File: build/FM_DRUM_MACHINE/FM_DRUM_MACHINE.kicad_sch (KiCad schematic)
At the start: 292 parts, among them J1 PJ-102A, J2 KICK_BUFFEREDOUT, J3 SNARE_BUFFEREDOUT, J4 HATS_BUFFEREDOUT, J5 TOMS_BUFFEREDOUT, J6 LINE_OUT, Q1 BC547, Q2 BC557, SW1 STEP1, SW10 STEP10, SW11 STEP11, SW12 STEP12, SW13 STEP13, SW14 STEP14, SW15 STEP15, SW16 STEP16, SW17 KICK_TRIG, SW18 SNARE_TRIG, SW19 CHAT_TRIG, SW2 STEP2, SW20 OHAT_TRIG, SW21 LOTOM_TRIG, SW22 HITOM_TRIG, SW23 PLAY/PAUSE, SW24 RECORD, SW25 SELECT, SW26 SW_DPDT_x2, SW27 SW_DPDT_x2, SW3 STEP3, SW4 STEP4, SW5 STEP5, SW6 STEP6, SW7 STEP7, SW8 STEP8, SW9 STEP9, U1 6N138, U10 TL072, U11 TL074, U12 TL072, U13 TL074, U14 TL074, U15 TL072, U16 TL072, U2 TL072, U3 TL072, U4 TL074, U5 MAX7221xNG, U6 CD74HC4067M, U7 CD74HC4067M, U8 AMS1117-5.0, U9 AMS1117-3.3

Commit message: v0.5.3
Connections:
- net HATS_DCBIAS_OUT is gone; now on net HATSBUFFER_IN: C5.1, R3.1, R4.2, R40.1
- net KICK_DCBIAS_OUT is gone; now on net KICKBUFFER_IN: C3.1, R38.1, R49.1, R50.2
- net SNARE_DCBIAS_OUT is gone; now on net SNAREBUFFER_IN: C4.1, R1.1, R2.2, R39.1
- net TOMS_DCBIAS_OUT is gone; now on net TOMSBUFFER_IN: C6.1, R41.1, R5.1, R6.2
- net HATSBUFFER_IN: no longer C5.2, RV33.3
- net KICKBUFFER_IN: no longer C3.2, RV46.3
- net SNAREBUFFER_IN: no longer RV40.3
- net TOMSBUFFER_IN: no longer C6.2, RV35.3
- new net HATS_DCBIAS_IN: C5.2, RV33.3
- new net KICK_DCBIAS_IN: C3.2, RV46.3
- new net SNARE_DCBIAS_IN: RV40.3
- new net TOMS_DCBIAS_IN: C6.2, RV35.3

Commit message: v0.5.5
- Drive section modified based on testing
- LPF/HPF Based on testing
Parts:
- removed D55, D56: 1N4148, Diode_THT:D_DO-35_SOD27_P5.08mm_Vertical_KathodeUp, symbol Diode:1N4148
- removed R42, R43, R47, R48, R49: 10k, PCM_4ms_Resistor:R_Axial_DIN0207_L6.3mm_D2.5mm_P7.62mm_Horizontal, symbol Device:R
- added R13: 820R, PCM_4ms_Resistor:R_Axial_DIN0207_L6.3mm_D2.5mm_P7.62mm_Horizontal, symbol Device:R
- added R14, R15: 330R, PCM_4ms_Resistor:R_Axial_DIN0207_L6.3mm_D2.5mm_P7.62mm_Horizontal, symbol Device:R
- D3: value 1N4148 -> RED LED
- D4: value 1N4148 -> 1N4007
- R1, R3, R5: value 10k -> 820R
- R2, R4, R50, R6: value 10k -> 330R
- R52: value 2k -> 680R
- R53, R56, R60, R73: value 200k -> 220k
- R58, R64: value 6k8 -> 10k
- RV29: value R_Potentiometer -> 100k
- RV38: value 20k -> B20k
- RV39: value 1k -> A1k
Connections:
- net 12V: no longer R1.2, R3.2, R5.2
- net GND: no longer R2.1, R4.1, R50.1, R6.1
- net HATSBUFFER_IN: no longer R3.1
- net SNAREBUFFER_IN: no longer R1.1
- net SOFTCLIP_OUT: now also D3.2 (A), D4.1 (K); no longer D4.2 (A)
- net TOMSBUFFER_IN: no longer R5.1
- net VGND: now also R2.1, R4.1, R5.2, R50.1, R6.1, RV38.3, U2.3 (+), U2.5 (+), R14.1, R15.1; no longer R52.1, RV27.1, RV29.1, TRIM1.1 (Left)
- net at D3.1 (K), R51.2, U3.2 (-): now also D4.2 (A), R52.2; no longer RV38.3
- net at RV27.4, U11.6 (-), U11.7: now also R13.1, R13.2
- net at U4.1, U4.2 (-): now also R1.1; no longer RV28.1
- net at RV28.4, U4.6 (-), U4.7: now also R3.1, R3.2
- net at RV38.1, RV38.2: now also R52.1; no longer R52.2
- new net: R5.1, RV27.1
- new net: R15.2, TRIM1.1 (Left)
- new net: R14.2, RV29.1
- new net: R1.2, RV28.1
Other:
- moved on the sheet: C3, C4, C5, C6, C82, C83, D3, D57, D58, D59, D60, D61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

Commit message: v0.6
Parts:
- R88: value 20k -> 33k
- RV31: value 20k -> 10k
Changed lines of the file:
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@@
 			)
 		)
-		(property "Value" "20k"
+		(property "Value" "33k"
 			(at 659.13 223.266 90)
 			(effects
@@
 			)
 		)
-		(property "Value" "20k"
+		(property "Value" "10k"
 			(at 661.67 234.9499 0)
 			(effects

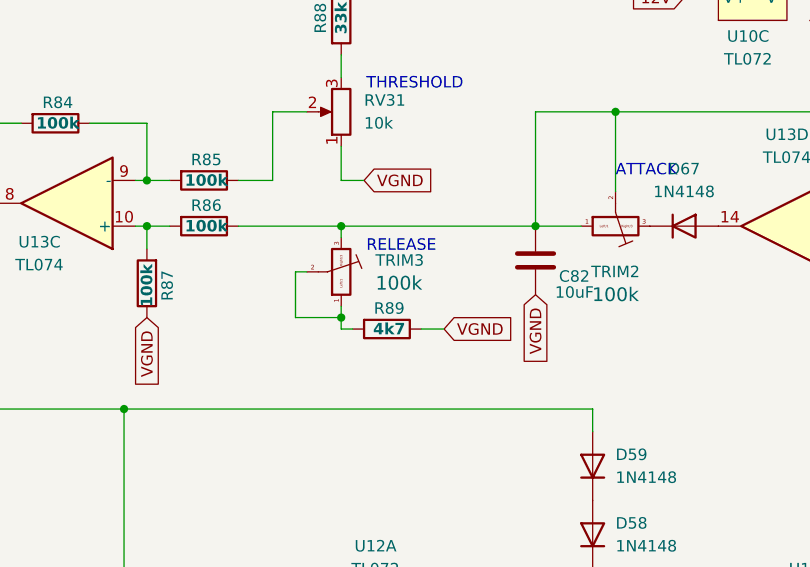
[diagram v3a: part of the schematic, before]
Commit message: Sound Design Edits
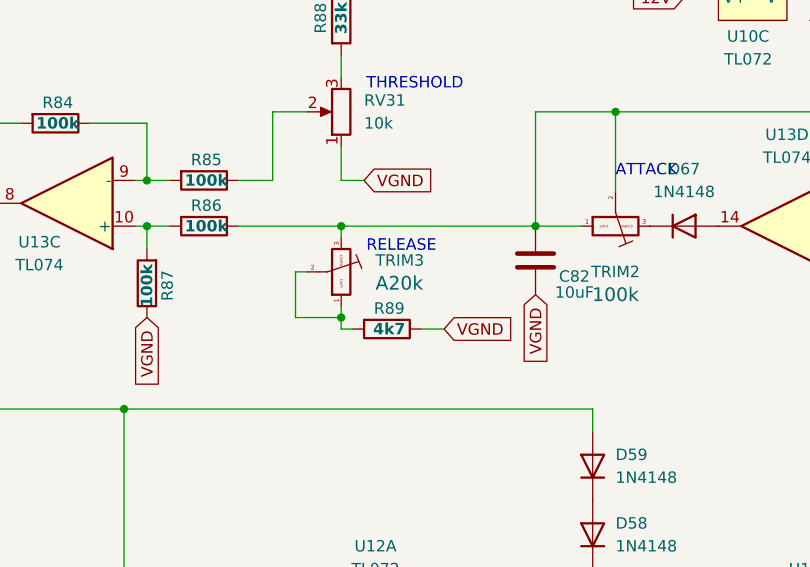
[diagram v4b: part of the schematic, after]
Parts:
- TRIM3: Display 100k -> A20k
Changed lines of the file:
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@@
 			)
 		)
-		(property "Display" "100k"
+		(property "Display" "A20k"
 			(at 662.94 252.7299 0)
 			(effects

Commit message: Schematic Changes
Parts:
- removed C65, C66, C67, C68: 10nF, PCM_4ms_Capacitor:C_Disc_P5.08mm, symbol Device:C
- removed RV23: OHAT_DECAY, DIYSynthMNL:Potentiometer_RV09_BigPads, symbol Device:R_Potentiometer
- removed RV24: OHAT_TIMBRE, DIYSynthMNL:Potentiometer_RV09_BigPads, symbol Device:R_Potentiometer
- removed RV25: OHAT_PITCH, DIYSynthMNL:Potentiometer_RV09_BigPads, symbol Device:R_Potentiometer
- removed RV26: OHAT_FMFREQ, DIYSynthMNL:Potentiometer_RV09_BigPads, symbol Device:R_Potentiometer
- RV11: value CHAT_DECAY -> HAT_DECAY
- RV12: value CHAT_TIMBRE -> HAT_TIMBRE
- RV13: value CHAT_PITCH -> HAT_TONE
- RV14: value CHAT_FMFREQ -> HAT_RESONANCE
- RV17: value LOTOM_PITCH -> LOTOM_TUNE
- RV18: value LOTOM_FMFREQ -> LOTOM_PITCHENVTIME
- RV21: value HITOM_PITCH -> HITOM_TUNE
- RV22: value HITOM_FMFREQ -> HITOM_PITCHENVTIME
- RV3: value KICK_PITCH -> KICK_TUNE
- RV5: value KICK_FMFREQ -> KICK_PITCHENVTIME
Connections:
- net OHAT_FMFREQ is gone; now on net LOTOM_DECAY: U7.9 (I0)
- net HITOM_DECAY: now also U7.5 (I4); no longer U7.4 (I5)
- net HITOM_PITCH: now also U7.4 (I5); no longer U7.3 (I6)
- net HITOM_PUNCH: now also U7.3 (I6); no longer U7.2 (I7)
- net LOTOM_DECAY: no longer U7.8 (I1)
- net LOTOM_PUNCH: now also U7.7 (I2); no longer U7.6 (I3)
- net CHAT_DECAY renamed HAT_DECAY
- net CHAT_FMFREQ renamed HAT_RESONANCE
- net CHAT_PITCH renamed HAT_TONE
- net CHAT_TIMBRE renamed HAT_TIMBRE
- net HITOM_FMFREQ renamed HITOM_PITCHENVTIME
- net HITOM_PITCHENVTIME: now also U7.2 (I7); no longer U7.23 (I8)
- net KICK_FMFREQ renamed KICK_PITCHENVTIME
- net KICK_PITCH renamed KICK_TUNE
- net LOTOM_FMFREQ renamed LOTOM_PITCHENVTIME
- net LOTOM_PITCHENVTIME: now also U7.6 (I3); no longer U7.5 (I4)
- net LOTOM_PITCH renamed LOTOM_TUNE
- net LOTOM_TUNE: now also U7.8 (I1); no longer U7.7 (I2)
- net OHAT_DECAY: no longer names the net of U6.18 (I13)
- net OHAT_PITCH: no longer names the net of U6.17 (I14)
- net OHAT_TIMBRE: no longer names the net of U6.16 (I15)
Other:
- note added: "HAT"
- note removed: "CHAT"
- note removed: "OHAT"

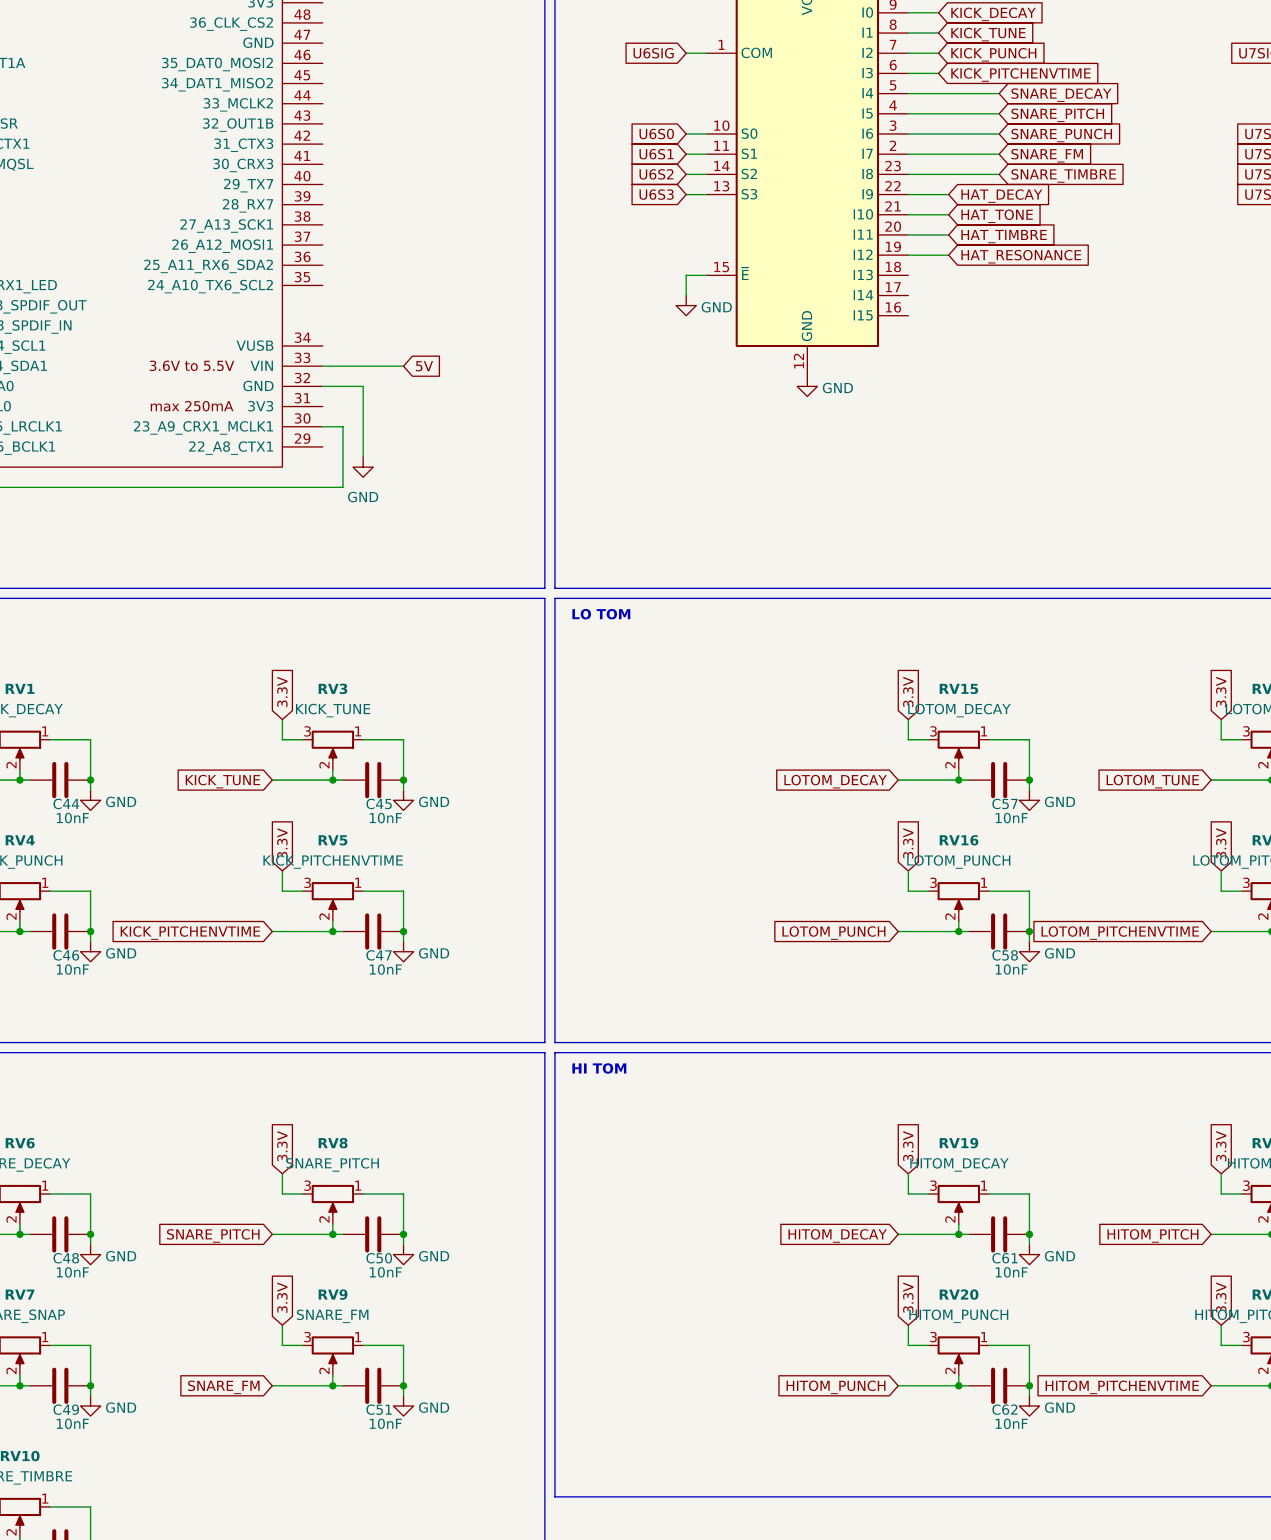
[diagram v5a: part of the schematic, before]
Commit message: Hi Hats added to ENGINE
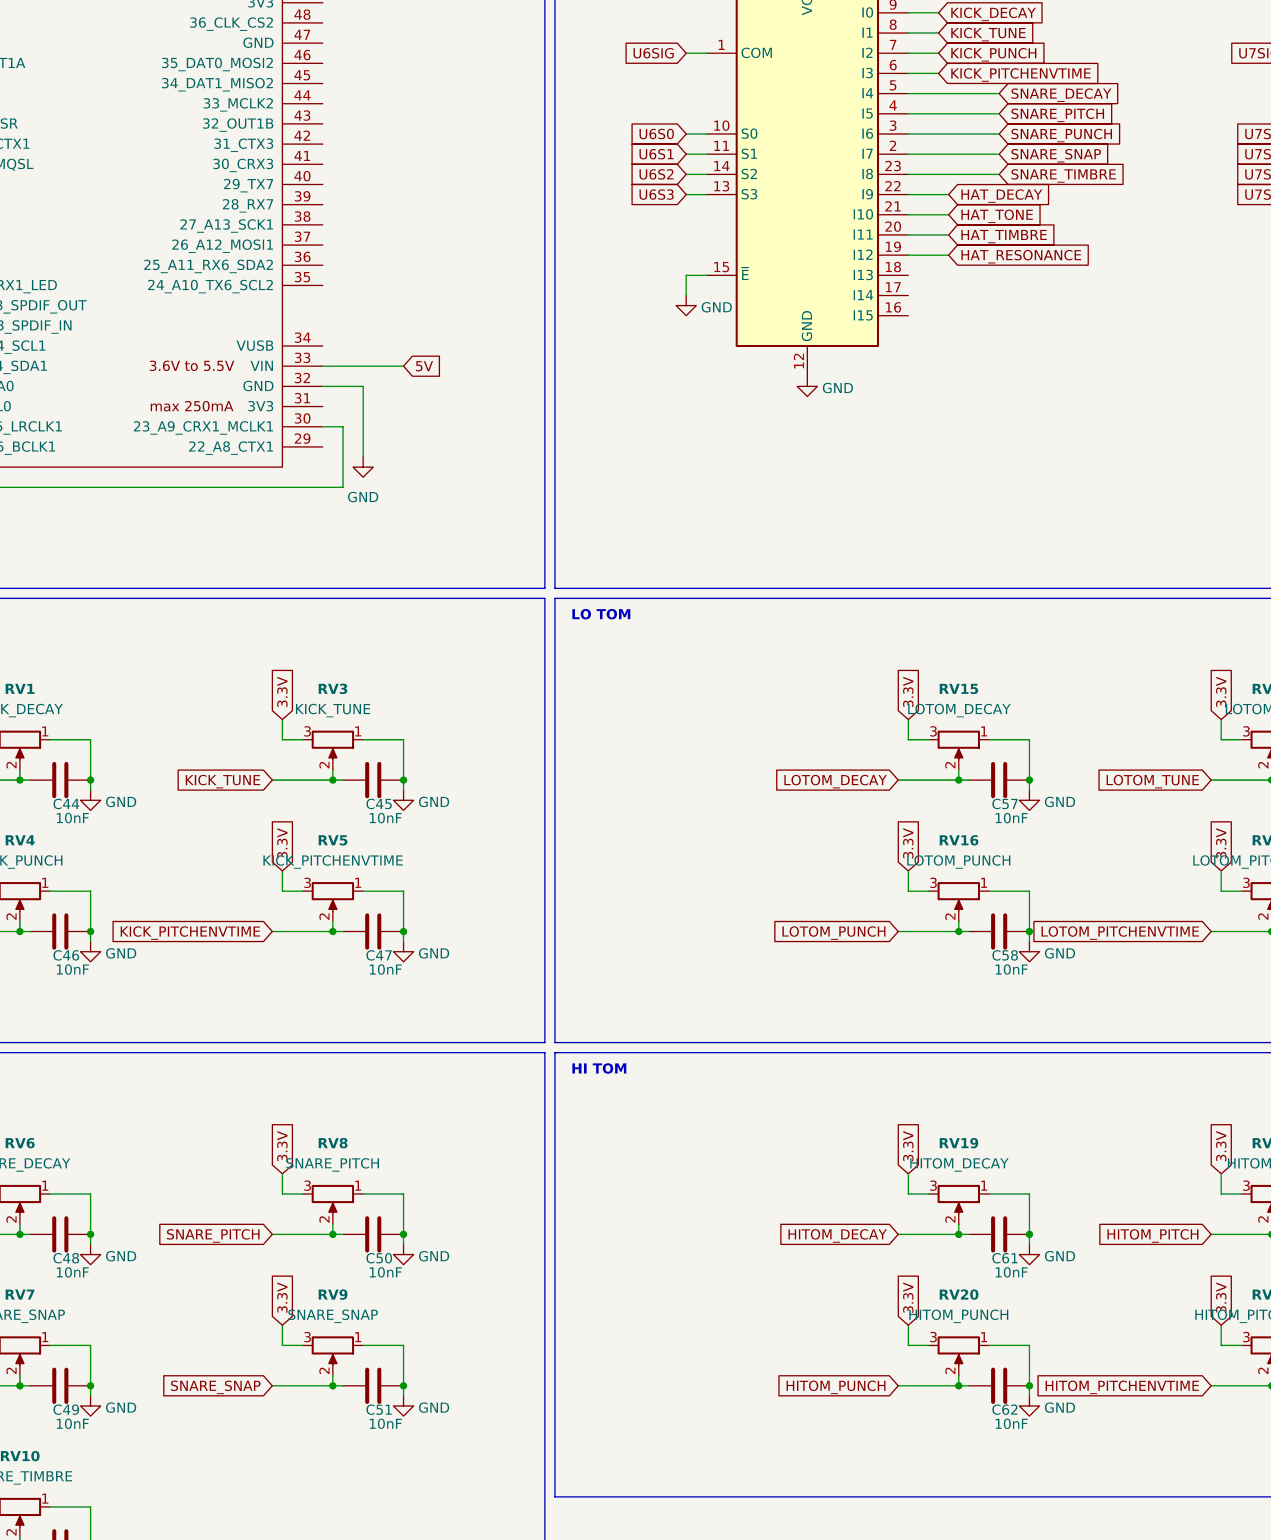
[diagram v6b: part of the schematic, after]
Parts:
- RV9: value SNARE_FM -> SNARE_SNAP
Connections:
- net SNARE_FM renamed SNARE_SNAP
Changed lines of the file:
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@@
 		)
 	)
+	(global_label "SNARE_SNAP"
+		(shape input)
+		(at 377.19 83.82 0)
+		(fields_autoplaced yes)
+		(effects
+			(font
+				(size 1.27 1.27)
+			)
+			(justify left)
+		)
+		(property "Intersheetrefs" "${INTERSHEET_REFS}"
+			(at 392.089 83.82 0)
+			(effects
+				(font
+					(size 1.27 1.27)
+				)
+				(justify left)
+				(hide yes)
+			)
+		)
+	)
 	(global_label "DIG4"
 		(shape input)
@@
 		)
 	)
-	(global_label "SNARE_FM"
+	(global_label "SNARE_SNAP"
 		(shape input)
 		(at 285.75 238.76 180)
@@
 		)
 		(property "Intersheetrefs" "${INTERSHEET_REFS}"
-			(at 273.2096 238.76 0)
+			(at 270.851 238.76 0)
 			(effects
 				(font
@@
 		)
 	)
-	(global_label "SNARE_FM"
-		(shape input)
-		(at 377.19 83.82 0)
-		(fields_autoplaced yes)
-		(effects
-			(font
-				(size 1.27 1.27)
-			)
-			(justify left)
-		)
-		(property "Intersheetrefs" "${INTERSHEET_REFS}"
-			(at 389.7304 83.82 0)
-			(effects
-				(font
-					(size 1.27 1.27)
-				)
-				(justify left)
-				(hide yes)
-			)
-		)
-	)
 	(global_label "KICK_TUNE"
 		(shape input)
@@
 			)
 		)
-		(property "Value" "SNARE_FM"
+		(property "Value" "SNARE_SNAP"
 			(at 293.37 229.87 90)
 			(effects

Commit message: Ground Loop Isolation
- Filtered +12V to help with noise. This also filters the Vref rail
- Separated. the DGND from AGND
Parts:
- added C7: 100uF, Capacitor_THT:CP_Radial_D5.0mm_P2.00mm, symbol Device:C_Polarized_US
- added R16: 10R, PCM_4ms_Resistor:R_Axial_DIN0207_L6.3mm_D2.5mm_P7.62mm_Horizontal, symbol Device:R
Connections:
- net AGND_KICK is gone; now on net AGND: A1.8 (AGND), J2.S
- net AGND_SNARE is gone; now on net AGND: A1.10 (AGND), J3.S
- net AGND_TOMS is gone; now on net AGND: A2.10 (AGND), J5.S
- net 12V: now also R16.1; no longer C1.1, Q1.1 (C), R70.1, R88.1, U10.8 (V+), U11.4 (V+), U12.8 (V+), U13.4 (V+), U14.4 (V+), U15.8 (V+), U2.8 (V+), U3.8 (V+), U4.4 (V+)
- net GND: now also C7.2; no longer J6.S, R96.2, R97.2, R98.2, R99.2, RV33.1, RV35.1, RV39.1, RV40.1, RV46.1, U10.4 (V-), U11.11 (V-), U12.4 (V-), U13.11 (V-), U14.11 (V-), U15.4 (V-), U2.4 (V-), U4.11 (V-)
- net AGND_HATS renamed AGND
- net AGND: now also J6.S, R96.2, R97.2, R99.2, RV33.1, RV35.1, RV39.1, RV40.1, RV46.1, U10.4 (V-), U11.11 (V-), U12.4 (V-), U13.11 (V-), U14.11 (V-), U15.4 (V-), U2.4 (V-), U4.11 (V-)
- net VGND renamed Vref
- new net A12V: C1.1, C7.1, Q1.1 (C), R16.2, R70.1, R88.1, U10.8 (V+), U11.4 (V+), U12.8 (V+), U13.4 (V+), U14.4 (V+), U15.8 (V+), U2.8 (V+), U3.8 (V+), U4.4 (V+)
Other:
- moved on the sheet: C1, C2, C73, Q1, Q2, R70, R71, R72, U10A, U10C, U12C, U13E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

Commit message: Ground Isolation
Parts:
- RV18: value LOTOM_PITCHENVTIME -> LOTOM_ATTACK
- RV22: value HITOM_PITCHENVTIME -> HITOM_ATTACK
- RV5: value KICK_PITCHENVTIME -> KICK_ATTACK
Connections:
- net HITOM_PITCHENVTIME renamed HITOM_ATTACK
- net KICK_PITCHENVTIME renamed KICK_ATTACK
- net LOTOM_PITCHENVTIME renamed LOTOM_ATTACK
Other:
- company: (none) -> .axs instruments
- title: (none) -> FM Drum Machine
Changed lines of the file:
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@@
 	(generator_version "9.0")
 	(paper "A0")
+	(title_block
+		(title "FM Drum Machine")
+		(company ".axs instruments")
+	)
 	(rectangle
 		(start 439.42 139.7)
@@
 	)
 	(junction
-		(at 518.16 147.32)
-		(diameter 0)
-		(color 0 0 0 0)
-	)
-	(junction
 		(at 718.82 127)
 		(diameter 0)
@@
 	)
 	(junction
+		(at 505.46 149.86)
+		(diameter 0)
+		(color 0 0 0 0)
+	)
+	(junction
 		(at 497.84 523.24)
 		(diameter 0)
@@
 	)
 	(junction
+		(at 518.16 149.86)
+		(diameter 0)
+		(color 0 0 0 0)
+	)
+	(junction
 		(at 91.44 46.99)
 		(diameter 0)
@@
 	)
 	(junction
-		(at 505.46 147.32)
-		(diameter 0)
-		(color 0 0 0 0)
-	)
-	(junction
 		(at 302.26 162.56)
 		(diameter 0)
@@
 	(wire
 		(pts
-			(xy 505.46 147.32) (xy 518.16 147.32)
+			(xy 505.46 149.86) (xy 518.16 149.86)
 		)
 		(stroke
@@
 	(wire
 		(pts
-			(xy 497.84 147.32) (xy 497.84 160.02)
+			(xy 497.84 149.86) (xy 497.84 160.02)
 		)
 		(stroke
@@
 	(wire
 		(pts
-			(xy 497.84 147.32) (xy 505.46 147.32)
+			(xy 497.84 149.86) (xy 505.46 149.86)
 		)
 		(stroke
@@
 	(wire
 		(pts
+			(xy 518.16 149.86) (xy 518.16 200.66)
+		)
+		(stroke
+			(width 0)
+			(type default)
+		)
+	)
+	(wire
+		(pts
 			(xy 283.21 360.68) (xy 283.21 382.27)
 		)
@@
 	(wire
 		(pts
-			(xy 518.16 147.32) (xy 538.48 147.32)
+			(xy 518.16 149.86) (xy 538.48 149.86)
 		)
 		(stroke
@@
 	(wire
 		(pts
-			(xy 505.46 147.32) (xy 505.46 160.02)
-		)
-		(stroke
-			(width 0)
-			(type default)
-		)
-	)
-	(wire
-		(pts
 			(xy 323.85 598.17) (xy 323.85 584.2)
 		)
@@
 	(wire
 		(pts
-			(xy 518.16 147.32) (xy 518.16 200.66)
-		)
-		(stroke
-			(width 0)
-			(type default)
-		)
-	)
-	(wire
-		(pts
 			(xy 472.44 497.84) (xy 474.98 497.84)
 		)
@@
 	(wire
 		(pts
+			(xy 505.46 149.86) (xy 505.46 160.02)
+		)
+		(stroke
+			(width 0)
+			(type default)
+		)
+	)
+	(wire
+		(pts
 			(xy 280.67 408.94) (xy 294.64 408.94)
 		)
@@
 		)
 	)
+	(global_label "KICK_ATTACK"
+		(shape input)
+		(at 285.75 181.61 180)
+		(fields_autoplaced yes)
+		(effects
+			(font
+				(size 1.27 1.27)
+			)
+			(justify right)
+		)
+		(property "Intersheetrefs" "${INTERSHEET_REFS}"
+			(at 270.73 181.61 0)
+			(effects
+				(font
+					(size 1.27 1.27)
+				)
+				(justify right)
+				(hide yes)
+			)
+		)
+	)
 	(global_label "Vref"
 		(shape input)
@@
 	(global_label "AGND"
 		(shape input)
-		(at 538.48 147.32 0)
+		(at 538.48 149.86 0)
 		(fields_autoplaced yes)
 		(effects
@@
 		)
 		(property "Intersheetrefs" "${INTERSHEET_REFS}"
-			(at 546.4243 147.32 0)
+			(at 546.4243 149.86 0)
 			(effects
 				(font
@@
 		)
 	)
-	(global_label "KICK_PITCHENVTIME"
-		(shape input)
-		(at 285.75 181.61 180)
-		(fields_autoplaced yes)
-		(effects
-			(font
-				(size 1.27 1.27)
-			)
-			(justify right)
-		)
-		(property "Intersheetrefs" "${INTERSHEET_REFS}"
-			(at 264.1986 181.61 0)
-			(effects
-				(font
-					(size 1.27 1.27)
-				)
-				(justify right)
-				(hide yes)
-			)
-		)
-	)
 	(global_label "KICK_DCBIAS_IN"
 		(shape input)
@@
 		)
 	)
-	(global_label "LOTOM_PITCHENVTIME"
+	(global_label "LOTOM_ATTACK"
 		(shape input)
 		(at 403.86 181.61 180)
@@
 		)
 		(property "Intersheetrefs" "${INTERSHEET_REFS}"
-			(at 380.6153 181.61 0)
+			(at 387.1467 181.61 0)
 			(effects
 				(font
@@
 		)
 	)
-	(global_label "HITOM_PITCHENVTIME"
+	(global_label "HITOM_ATTACK"
 		(shape input)
 		(at 447.04 83.82 0)
@@
 		)
 		(property "Intersheetrefs" "${INTERSHEET_REFS}"
-			(at 469.8614 83.82 0)
+			(at 463.33 83.82 0)
 			(effects
 				(font
@@
 		)
 	)
-	(global_label "KICK_PITCHENVTIME"
+	(global_label "KICK_ATTACK"
 		(shape input)
 		(at 369.57 73.66 0)
@@
 		)
 		(property "Intersheetrefs" "${INTERSHEET_REFS}"
-			(at 391.1214 73.66 0)
+			(at 384.59 73.66 0)
 			(effects
 				(font
@@
 		)
 	)
-	(global_label "LOTOM_PITCHENVTIME"
+	(global_label "LOTOM_ATTACK"
 		(shape input)
 		(at 454.66 73.66 0)
@@
 		)
 		(property "Intersheetrefs" "${INTERSHEET_REFS}"
-			(at 477.9047 73.66 0)
+			(at 471.3733 73.66 0)
 			(effects
 				(font
@@
 		)
 	)
-	(global_label "HITOM_PITCHENVTIME"
+	(global_label "HITOM_ATTACK"
 		(shape input)
 		(at 403.86 238.76 180)
@@
 		)
 		(property "Intersheetrefs" "${INTERSHEET_REFS}"
-			(at 381.0386 238.76 0)
+			(at 387.57 238.76 0)
 			(effects
 				(font
@@
 			)
 		)
-		(property "Value" "HITOM_PITCHENVTIME"
+		(property "Value" "HITOM_ATTACK"
 			(at 411.48 229.87 90)
 			(effects
@@
 			)
 		)
-		(property "Value" "KICK_PITCHENVTIME"
+		(property "Value" "KICK_ATTACK"
 			(at 293.37 172.72 90)
 			(effects
@@
 			)
 		)
-		(property "Value" "LOTOM_PITCHENVTIME"
+		(property "Value" "LOTOM_ATTACK"
 			(at 411.48 172.72 90)
 			(effects
